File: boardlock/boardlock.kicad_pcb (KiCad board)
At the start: 2 copper layers, 127 x 76.2 mm, 179 parts, among them J1 Conn_01x02, J2 Conn_01x02, J3 5033981892, J4 Conn_01x02, J5 Conn_01x02, J6 USB_C_Receptacle_USB2.0, Q1 BSS84PWH6327XTSA1, Q2 MMBT4401, Q3 MMBT4401, Q4 BSS84PWH6327XTSA1, Q5 MMBT4401, Q6 MMBT4401, Q7 MMBT4401, Q8 BSS84PWH6327XTSA1, Q9 MMBT4401, SW1 SW_Push, SW2 SW_Push, SW3 SW_Push, SW4 SW_Push, SW5 SW_Push, U10 ESP32-S3-WROOM-1, U2 LSM6DSO32, U3 SAM-M8Q, U4 BQ24075RGT, U5 BQ27441DRZR-G1A, U6 TPS630701RNMR, U7 MAX98357AETE+T, U8 MCP1661, U9 TPD2E2U06

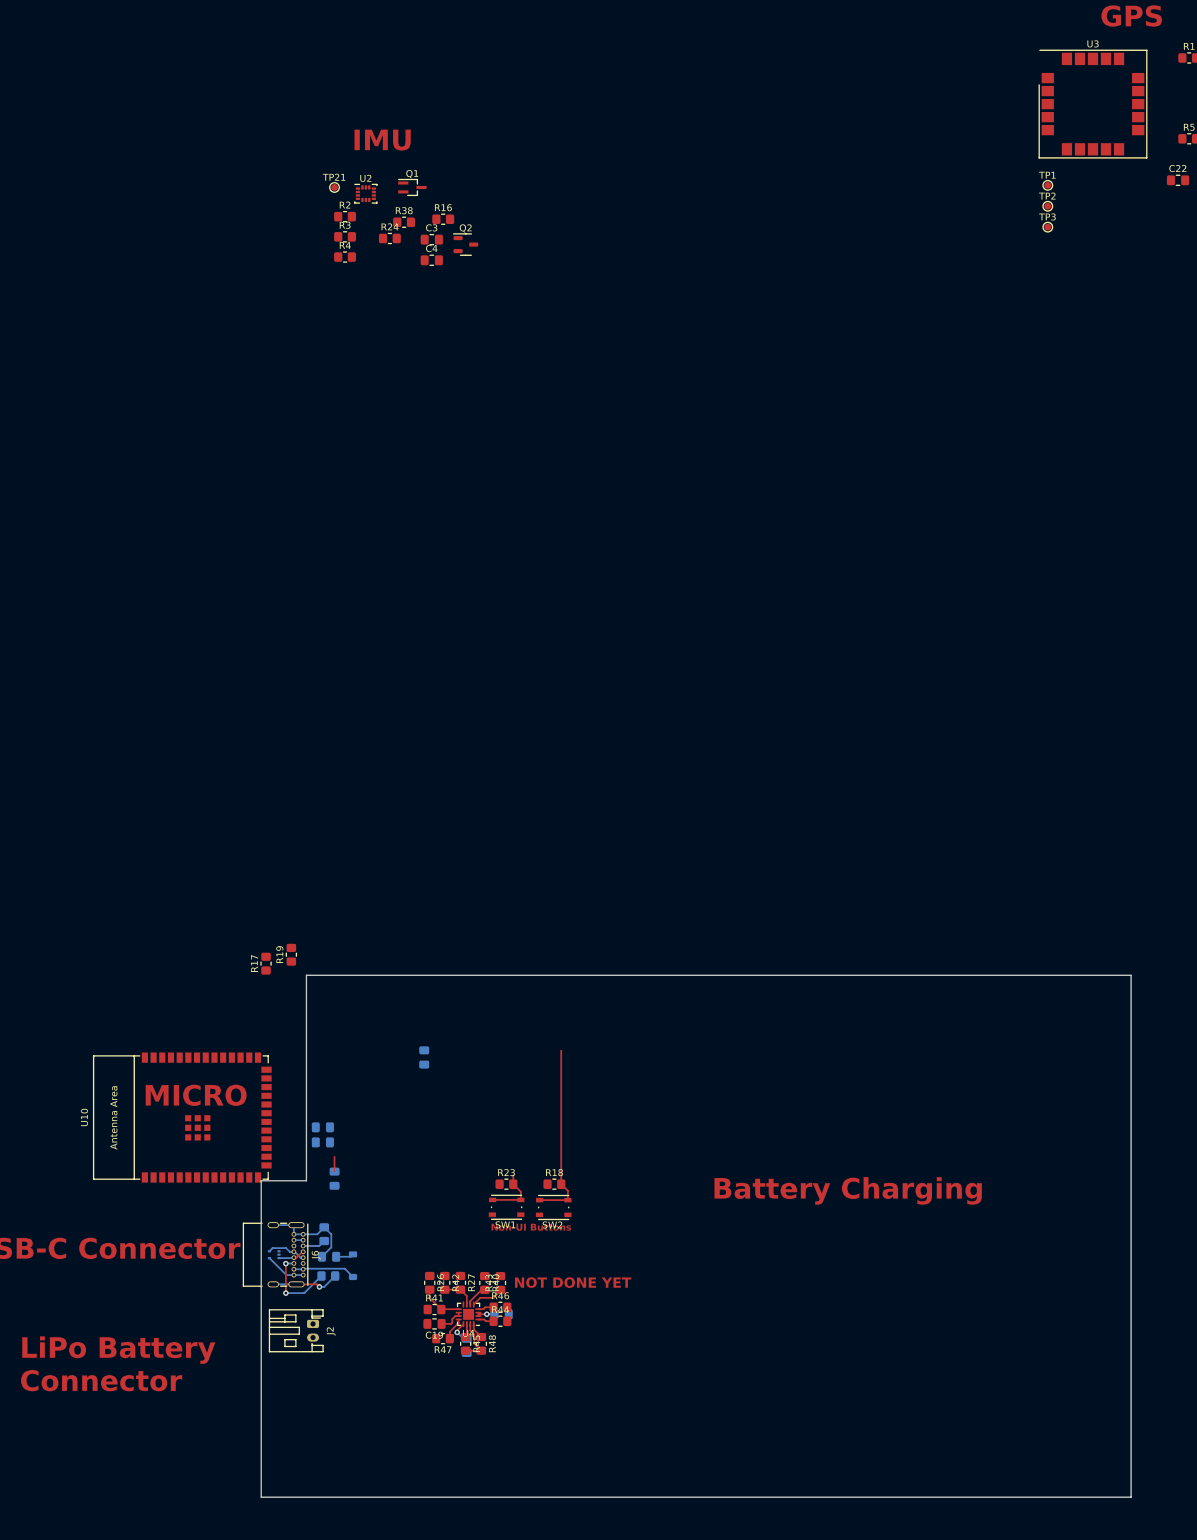
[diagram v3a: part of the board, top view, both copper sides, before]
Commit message: pad extensions for GPS and IMU, and IMU footprint added
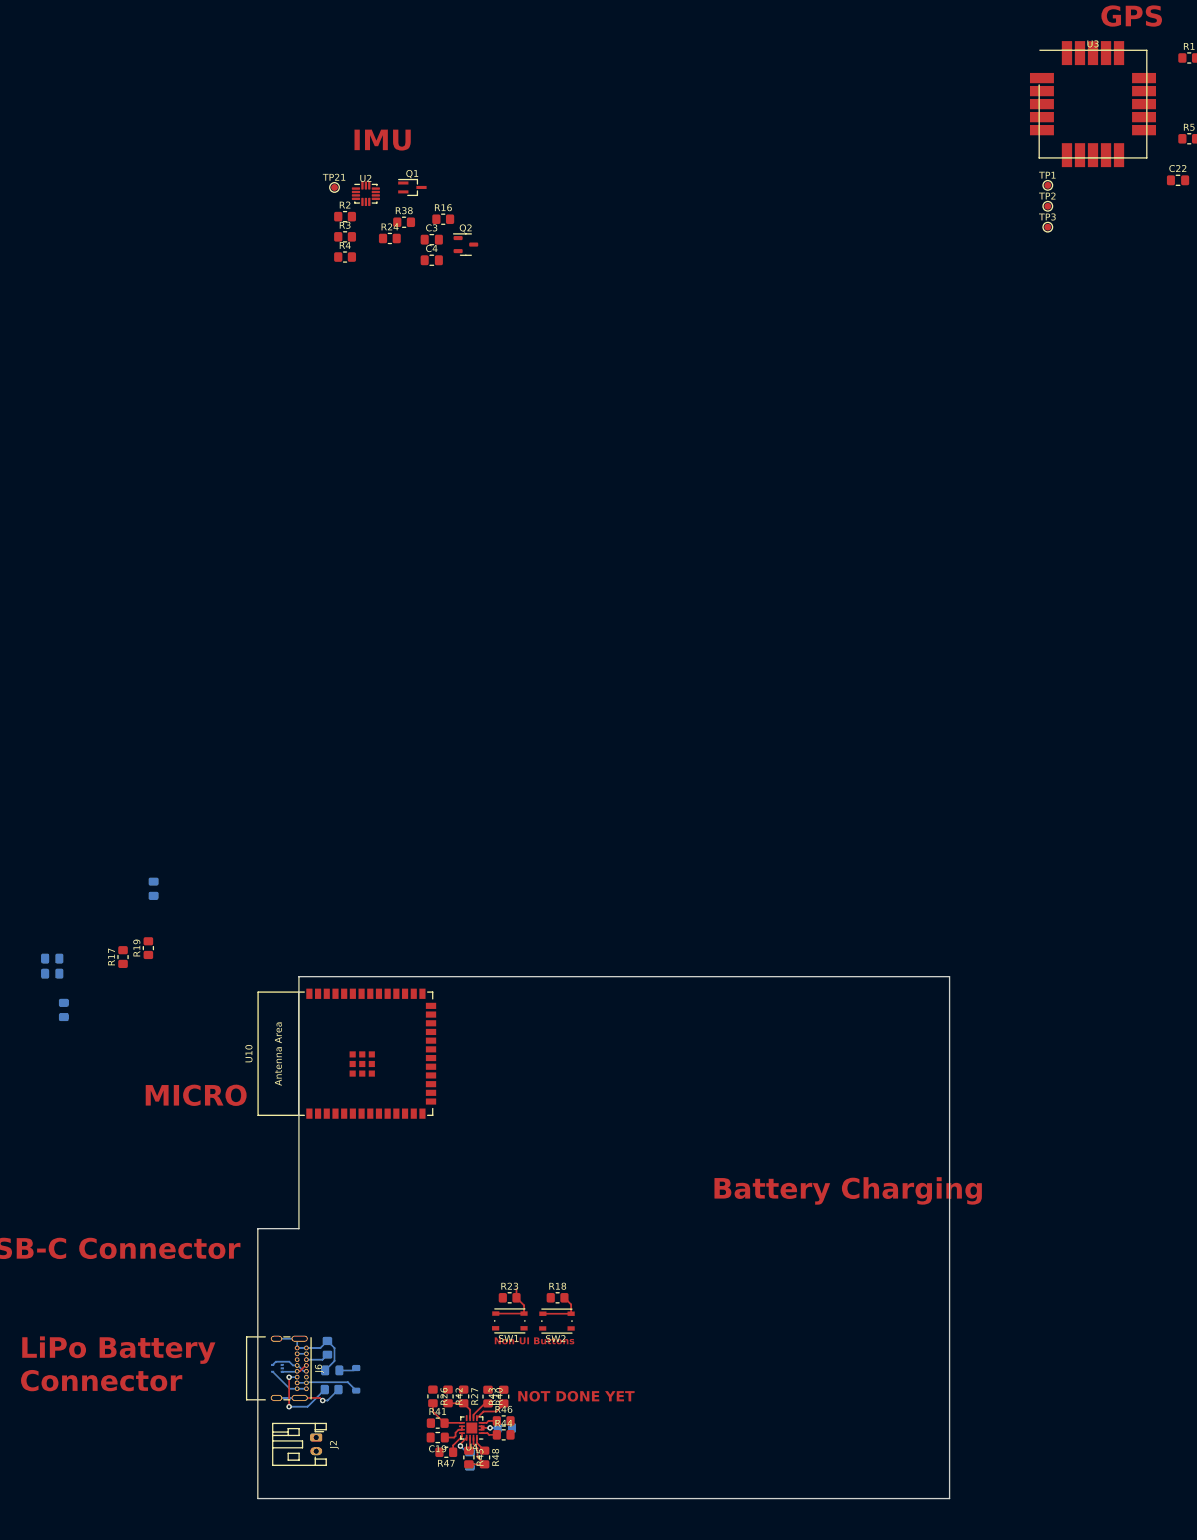
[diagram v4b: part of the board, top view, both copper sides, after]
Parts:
- moved C23 46.6 mm to (36.7, 42.1)
- moved C1 46.6 mm to (35.0, 34.6)
- moved C2 46.6 mm to (35.0, 36.8)
- moved C24 46.6 mm to (49.8, 24.4)
- moved U10 25.8 mm to (80.8, 48.5)
- moved R19 20.9 mm to (49.0, 33.0)
- moved R17 20.9 mm to (45.3, 34.3)
- moved C18 16.6 mm to (96.0, 107.7)
- moved C20 16.6 mm to (101.1, 103.1)
- moved C34 16.6 mm to (75.9, 94.7)
- moved J6 16.6 mm to (72.1, 91.4)
- moved R12 16.6 mm to (75.2, 91.4)
- moved R18 16.6 mm to (108.8, 84.1)
- moved R23 16.6 mm to (101.8, 84.1)
- moved R40 16.6 mm to (98.6, 98.5)
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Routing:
- net M_BOOT: track 26.4 -> 6.85 mm
- net M_RST_N: track 10.3 -> 8.18 mm
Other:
- board size 127 x 76.2 mm -> 101 x 76.2 mm

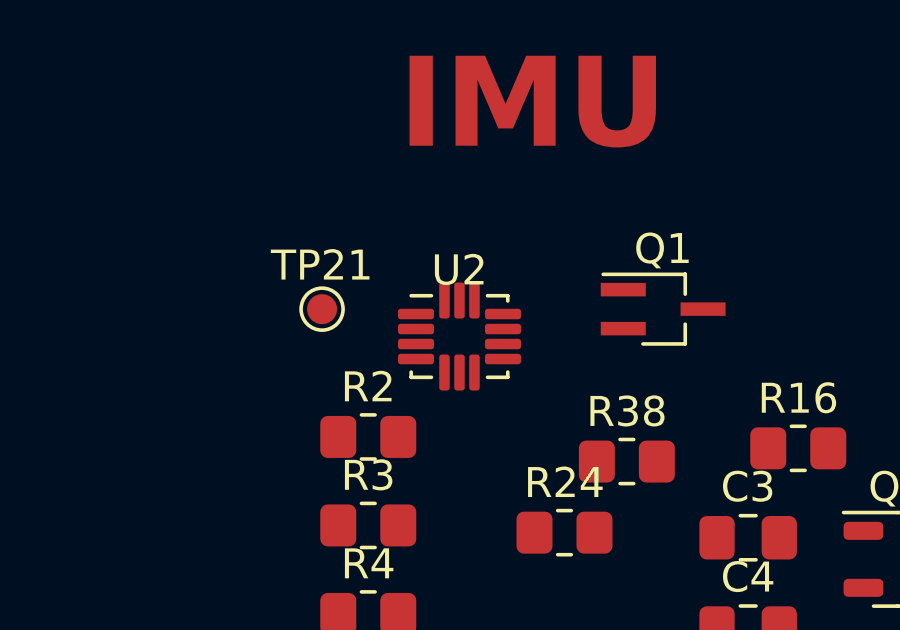
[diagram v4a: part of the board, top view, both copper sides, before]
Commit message: nevermind still need to extend IMU
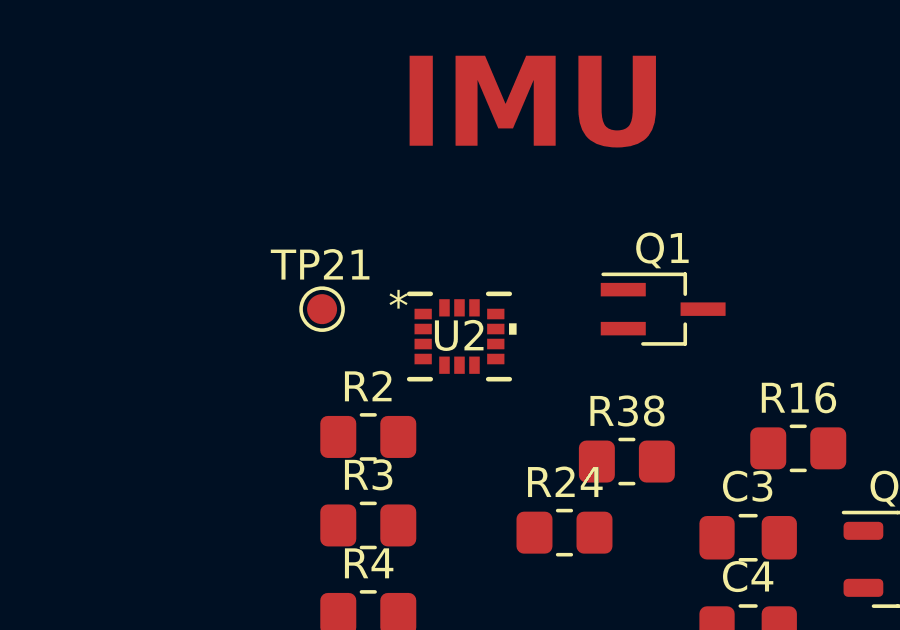
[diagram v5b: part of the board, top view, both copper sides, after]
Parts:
- U2: footprint Package_LGA:LGA-14_3x2.5mm_P0.5mm_LayoutBorder3x4y -> LSM6DSO32TR:LGA-14L_2P5X3X0P83_STM-L

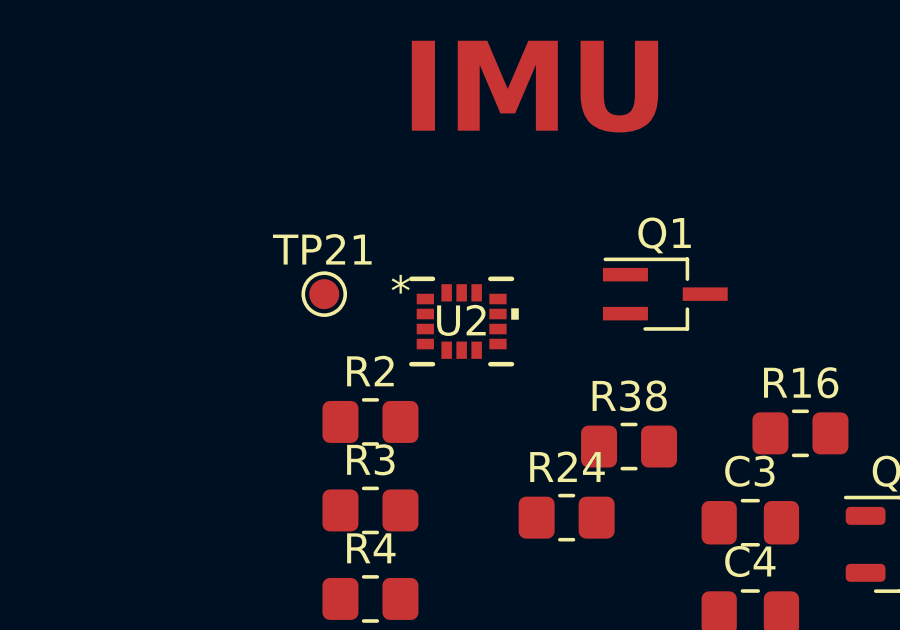
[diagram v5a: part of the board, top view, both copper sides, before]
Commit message: changed IMU footprint to extended pads
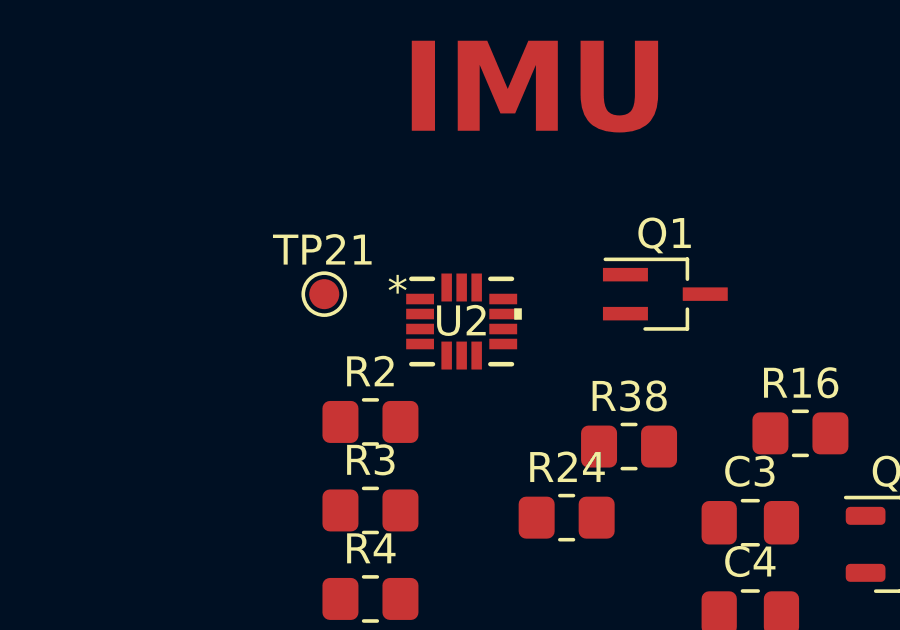
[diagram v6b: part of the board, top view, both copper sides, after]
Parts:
- U2: footprint LSM6DSO32TR:LGA-14L_2P5X3X0P83_STM-L -> LSM6DSO32TR:LGA-14L_2P5X3X0P83_STM-M

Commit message: PCB: added keep out areas on edge
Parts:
- moved J2 206.3 mm to (269.4, 39.6)
- moved J6 95.3 mm to (159.9, 54.4), turned to 90 degrees
- moved C19 86.9 mm to (24.6, 160.3)
- moved R27 86.9 mm to (28.4, 154.3)
- moved R40 86.9 mm to (32.0, 154.3)
- moved R41 86.9 mm to (24.6, 158.2)
- moved R42 86.9 mm to (26.1, 154.3)
- moved R43 86.9 mm to (34.2, 154.3)
- moved R44 86.9 mm to (34.2, 159.9)
- moved R46 86.9 mm to (34.2, 157.9)
- moved R47 86.9 mm to (25.9, 162.4)
- moved R48 86.9 mm to (31.5, 163.2)
- moved SW2 86.9 mm to (42.0, 143.3)
- moved C18 86.9 mm to (29.3, 163.5)
- moved C20 86.9 mm to (34.4, 158.9)
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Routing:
- net GND: track 37.6 -> 6.82 mm, vias 1 -> 0
- net Net-(J6-CC2): track 11.7 -> 0.00 mm, vias 2 -> 0
- net /ui/V_USB: track 10.5 -> 0.00 mm
- net USB_D-: track 5.70 -> 0.00 mm
- net USB_D+: track 3.91 -> 0.00 mm
- net Net-(J6-CC1): track 3.38 -> 0.00 mm
- net VBUS: track 5.95 -> 3.34 mm

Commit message: Repositioned USB C port
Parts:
- C1, C2, U9: moved to F.Cu
- C29: renamed from C23; moved to F.Cu
- C30: renamed from C24; moved to F.Cu
- D3: renamed from D2; moved to F.Cu
- moved C30 110.7 mm to (37.3, 134.3)
- moved C29 92.9 mm to (30.0, 134.7), turned to 180 degrees
- moved C1 49.5 mm to (75.5, 62.9)
- moved C2 47.2 mm to (75.5, 60.9)
- moved D3 16.9 mm to (156.0, 57.7)
- moved U9 13.3 mm to (156.5, 51.9), turned to 0 degrees
- renumbered C25 to C10, C10 to C11, C11 to C12, C12 to C13, C5 to C14, C6 to C15, C7 to C16, C9 to C17, C8 to C18, C29 to C19, C16 to C20, C15 to C21, C17 to C22, C30 to C23, C13 to C24, C14 to C25, C31 to C26, C32 to C27, C33 to C28, C34 to C31, C26 to C32, C28 to C33, C27 to C34, C22 to C5, C18 to C6, C20 to C7, C19 to C8, C21 to C9, D3 to D1, D1 to D2, J2 to J1, J1 to J2, J4 to J3, J5 to J4, J3 to J5, Q4 to Q2, Q2 to Q3, Q3 to Q4, Q8 to Q5, Q9 to Q6, Q5 to Q7, Q6 to Q8, Q7 to Q9, R17 to R1, R24 to R10, R25 to R11, R38 to R12, R1 to R13, R15 to R14, R7 to R15, R8 to R16, R2 to R17, R3 to R18, R28 to R19, R19 to R2, R40 to R20, R41 to R21, R42 to R22, R43 to R23, R44 to R24, R45 to R25, R46 to R26, R47 to R27, R48 to R28, R49 to R29, R26 to R3, R50 to R30, R51 to R31, R52 to R32, R53 to R33, R9 to R34, R14 to R35, R11 to R36, R10 to R37, R54 to R38, R55 to R39, R27 to R4, R56 to R40, R57 to R41, R58 to R42, R59 to R43, R60 to R44, R61 to R45, R23 to R46, R18 to R47, R12 to R48, R13 to R49, R29 to R5, R20 to R50, R22 to R51, R21 to R52, R31 to R53, R34 to R54, R37 to R55, R32 to R56, R33 to R57, R36 to R58, R39 to R59, R4 to R6, R30 to R60, R35 to R61, R6 to R7, R16 to R8, R5 to R9, TP16 to TP1, TP12 to TP10, TP17 to TP11, TP11 to TP12, TP18 to TP13, TP10 to TP14, TP34 to TP15, TP19 to TP16, TP20 to TP17, TP22 to TP18, TP23 to TP19, TP31 to TP2, TP24 to TP20, TP25 to TP21, TP26 to TP22, TP27 to TP23, TP28 to TP24, TP29 to TP25, TP35 to TP26, TP36 to TP27, TP37 to TP28, TP38 to TP29, TP32 to TP3, TP39 to TP30, TP30 to TP31, TP40 to TP32, TP9 to TP33, TP33 to TP34, TP43 to TP35, TP6 to TP36, TP41 to TP37, TP15 to TP38, TP42 to TP39, TP14 to TP4, TP1 to TP40, TP3 to TP41, TP2 to TP42, TP21 to TP43, TP4 to TP5, TP13 to TP6, TP5 to TP8, TP8 to TP9, U10 to U1, U3 to U2, U2 to U3, U8 to U7, U7 to U8
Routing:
- net +3V3: track 0.00 -> 6.83 mm
- net GND: track 6.82 -> 13.3 mm
- added copper zone on F.Cu, net GND
